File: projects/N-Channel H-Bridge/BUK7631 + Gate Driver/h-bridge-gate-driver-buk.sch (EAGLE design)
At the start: 24 parts, among them IC1 MIC5014YM, IC2 MIC5014YM, IC3 MIC5014YM, IC4 MIC5014YM, Q1 BUK7631, Q2 BUK7631, Q3 BUK7631, Q4 BUK7631'

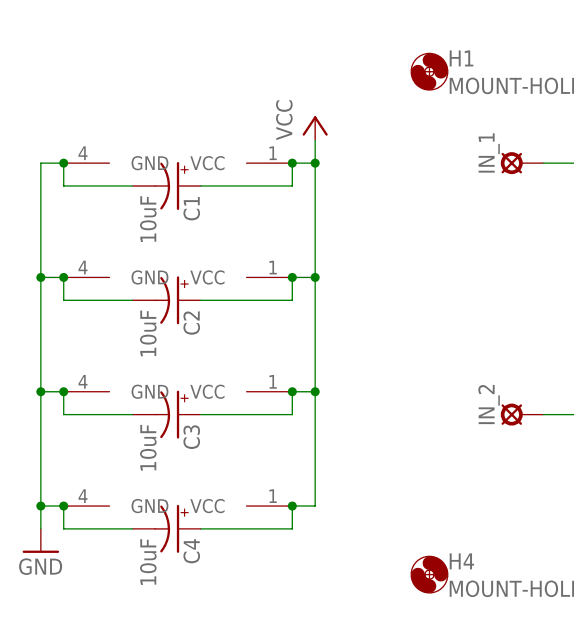
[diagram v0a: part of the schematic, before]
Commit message: replaced with the proper cap package
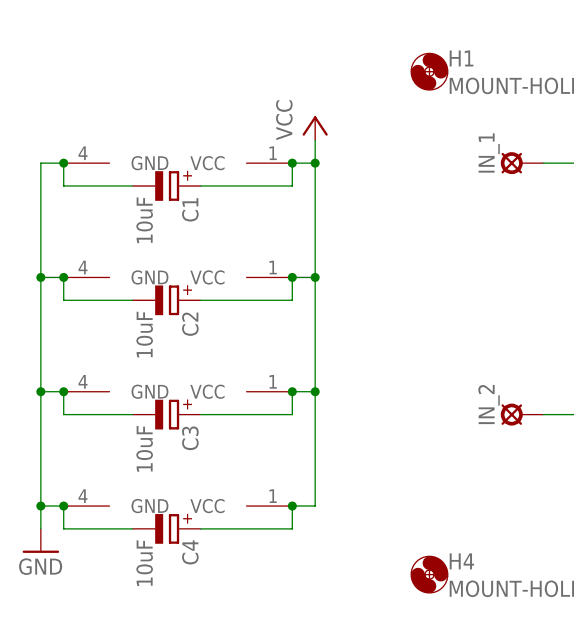
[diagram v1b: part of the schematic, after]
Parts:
- C1, C2, C3, C4: device adafruit:CPOL-US153CLV-0810 -> rcl:CPOL-EUUD-4X5,8
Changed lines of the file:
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@@
 <part name="IC4" library="nervus" deviceset="MIC5014" device="YM"/>
 <part name="GND4" library="supply1" deviceset="GND" device=""/>
-<part name="C1" library="adafruit" deviceset="CPOL-US" device="153CLV-0810" value="10uF"/>
-<part name="C2" library="adafruit" deviceset="CPOL-US" device="153CLV-0810" value="10uF"/>
-<part name="C3" library="adafruit" deviceset="CPOL-US" device="153CLV-0810" value="10uF"/>
-<part name="C4" library="adafruit" deviceset="CPOL-US" device="153CLV-0810" value="10uF"/>
+<part name="C1" library="rcl" deviceset="CPOL-EU" device="UD-4X5,8" value="10uF"/>
+<part name="C2" library="rcl" deviceset="CPOL-EU" device="UD-4X5,8" value="10uF"/>
+<part name="C3" library="rcl" deviceset="CPOL-EU" device="UD-4X5,8" value="10uF"/>
+<part name="C4" library="rcl" deviceset="CPOL-EU" device="UD-4X5,8" value="10uF"/>
 <part name="P+1" library="supply1" deviceset="VCC" device=""/>
 <part name="P+3" library="supply1" deviceset="VCC" device=""/>
